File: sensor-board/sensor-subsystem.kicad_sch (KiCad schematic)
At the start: 6 parts, among them J1 Conn_01x06_Pin, U1 VL53L0CXV0DH1

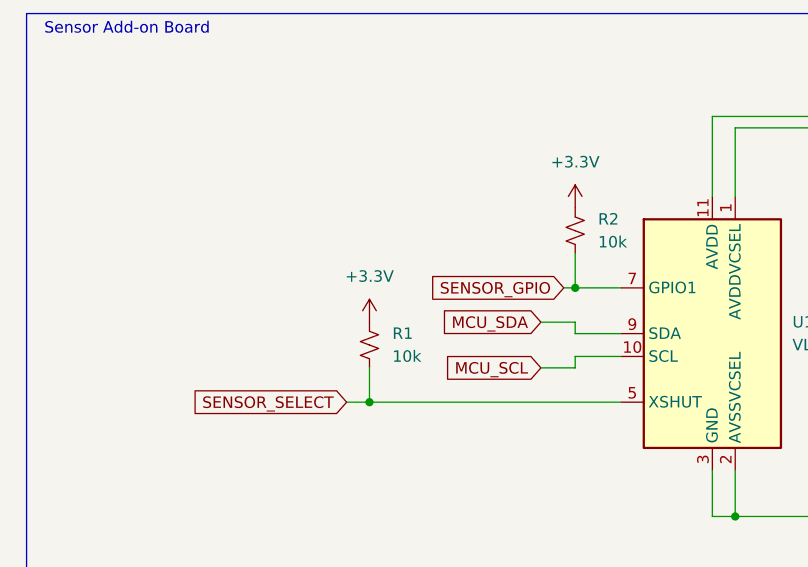
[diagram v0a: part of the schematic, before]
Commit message: improved sensor breakout board
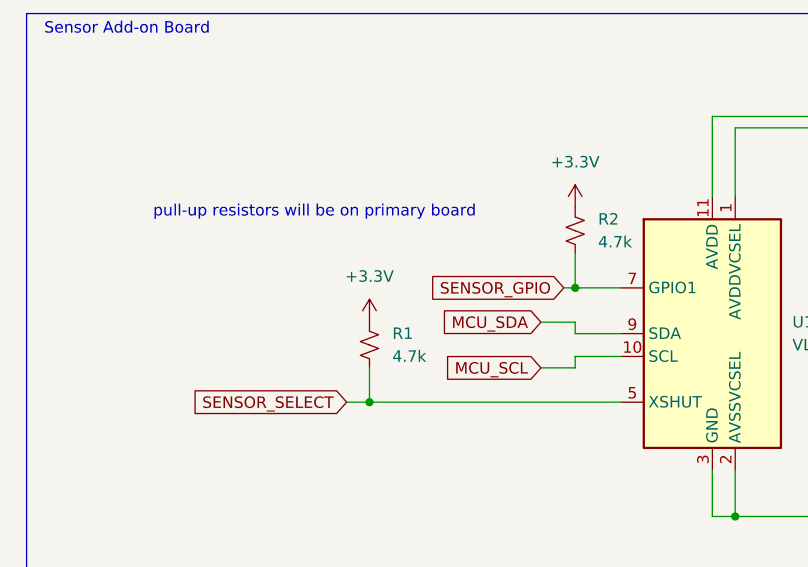
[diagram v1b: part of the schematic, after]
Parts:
- R1, R2: value 10k -> 4.7k
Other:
- note added: "pull-up resistors will be on primary board"
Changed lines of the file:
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@@
+		)
+	)
+	(text "pull-up resistors will be on primary board"
+		(exclude_from_sim no)
+		(at 44.704 34.798 0)
+		(effects
+			(font
+				(size 1.27 1.27)
+			)
 		)
 	)
@@
 			)
 		)
-		(property "Value" "10k"
+		(property "Value" "4.7k"
 			(at 53.34 50.7999 0)
 			(effects
@@
 			)
 		)
-		(property "Value" "10k"
+		(property "Value" "4.7k"
 			(at 76.2 38.0999 0)
 			(effects

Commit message: improved sensor board
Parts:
- added R3, R4: 10k, Resistor_SMD:R_0805_2012Metric, symbol Device:R_Small_US
- R1, R2: value 4.7k -> 10k
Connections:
- net +3.3V: now also R3.1, R4.2
- net MCU_SCL: now also R3.2
- net MCU_SDA: now also R4.1
